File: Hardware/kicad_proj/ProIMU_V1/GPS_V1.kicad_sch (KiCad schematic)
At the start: 14 parts, among them J2 221790-1

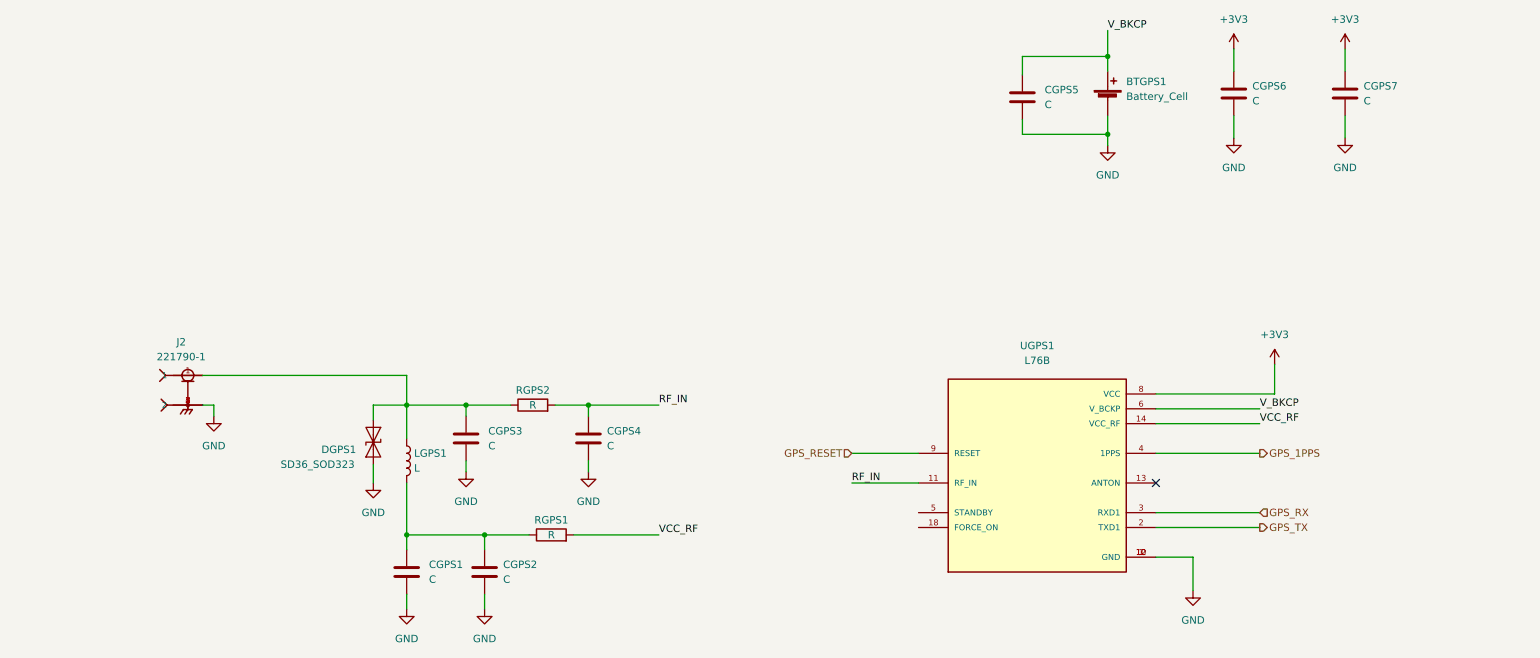
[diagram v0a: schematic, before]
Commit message: Added GPS, LoRa and Wifi v1 schematic blocks
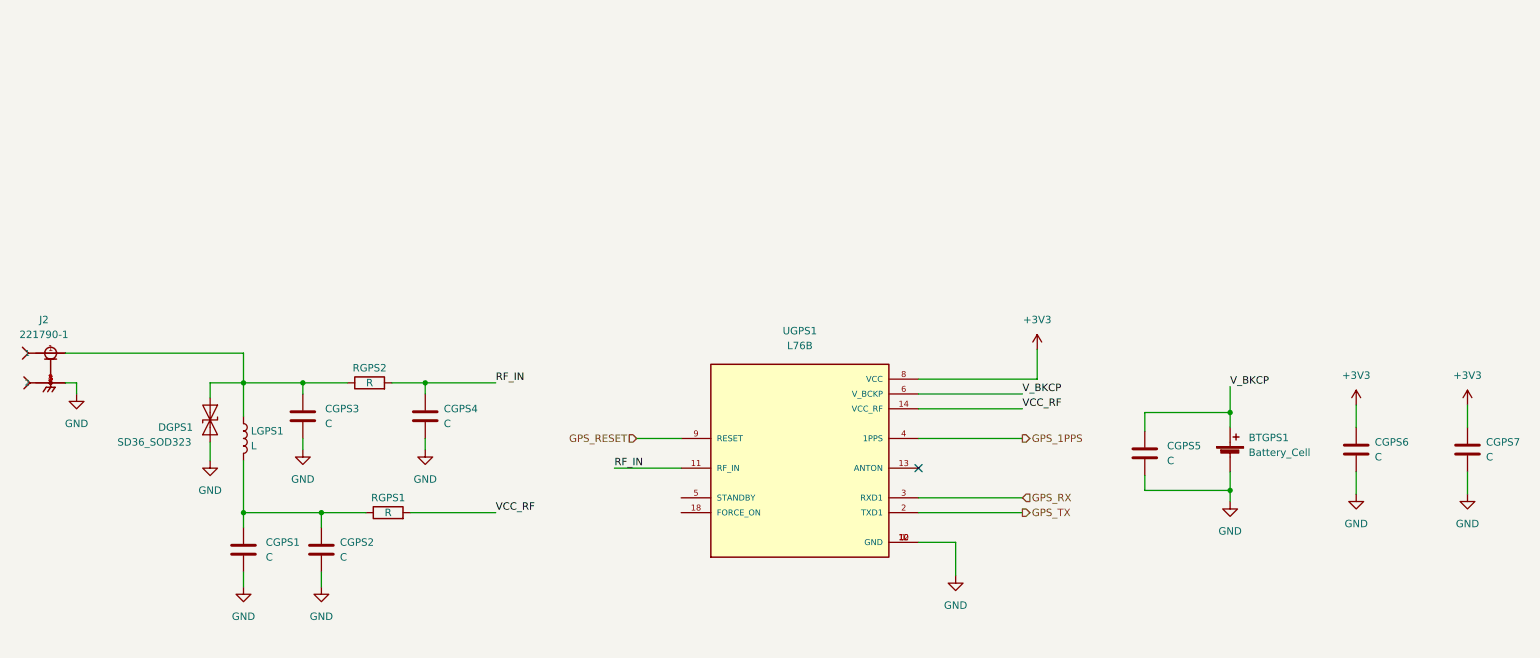
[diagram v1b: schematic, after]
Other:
- moved on the sheet: BTGPS1, CGPS1, CGPS2, CGPS3, CGPS4, CGPS5, CGPS6, CGPS7, DGPS1, J2, LGPS1, RGPS1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
